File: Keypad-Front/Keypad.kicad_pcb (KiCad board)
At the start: 4 copper layers, 100.1 x 192.1 mm, 43 parts, among them J2 LED BOARD 1, J3 LED BOARD 2, J4 LED BOARD 3, J5 LED BOARD 4, J6 Conn_01x06, U1 DS3231MZ

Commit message: Back to a one-board design with rear-firing LEDs
Giving up on the UV LED idea for now.
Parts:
- removed J2: LED BOARD 1, Connector_PinHeader_2.54mm:PinHeader_2x02_P2.54mm_Vertical_SMD
- removed J3: LED BOARD 2, Connector_PinHeader_2.54mm:PinHeader_2x02_P2.54mm_Vertical_SMD
- removed J4: LED BOARD 3, Connector_PinHeader_2.54mm:PinHeader_2x02_P2.54mm_Vertical_SMD
- removed J5: LED BOARD 4, Connector_PinHeader_2.54mm:PinHeader_2x02_P2.54mm_Vertical_SMD
- removed R16: 4.7k, Resistor_SMD:R_0805_2012Metric_Pad1.20x1.40mm_HandSolder
- added BT1: Battery_Cell, Battery:BatteryHolder_MPD_BC2003_1x2032, B.Cu at (143.8, 194.3)
- added J1: RTC STEMMA QT, Transflective:JST-SH-4-VERT-SMD, B.Cu at (125.5, 204.3)
- added TP10: TestPoint, Keypad:Touch_Pad_D1.0mm, F.Cu at (81.5, 155.5)
- added TP11: TestPoint, Keypad:Touch_Pad_D1.0mm, F.Cu at (106.5, 155.5)
- added TP12: TestPoint, Keypad:Touch_Pad_D1.0mm, F.Cu at (131.5, 155.5)
- added TP14: Guard, Keypad:Touch_Pad_D1.0mm, B.Cu at (70.4, 76.2)
- added TP2: TestPoint, Keypad:Touch_Pad_D1.0mm, F.Cu at (106.5, 80.5)
- added TP3: TestPoint, Keypad:Touch_Pad_D1.0mm, F.Cu at (131.5, 80.5)
- added TP4: TestPoint, Keypad:Touch_Pad_D1.0mm, F.Cu at (81.5, 105.5)
- added TP5: TestPoint, Keypad:Touch_Pad_D1.0mm, F.Cu at (106.5, 105.5)
- added TP6: TestPoint, Keypad:Touch_Pad_D1.0mm, F.Cu at (131.5, 105.5)
- added TP7: TestPoint, Keypad:Touch_Pad_D1.0mm, F.Cu at (81.5, 130.5)
- added TP8: TestPoint, Keypad:Touch_Pad_D1.0mm, F.Cu at (106.5, 130.5)
- added TP9: TestPoint, Keypad:Touch_Pad_D1.0mm, F.Cu at (131.5, 130.5)
- added U3: CAP1214, Package_DFN_QFN:QFN-32-1EP_5x5mm_P0.5mm_EP3.3x3.3mm_ThermalVias, B.Cu at (108.5, 68.8)
- C1, C4, R13, R14, R17, R18, R19, U1: moved to B.Cu
- R1, R10, R11, R12, R2, R3, R4, R5, R6, R7, R8, R9: value 4.7k -> 100; moved to B.Cu
- R15: value 4.7k -> 0; moved to B.Cu
- TP1: value Guard -> TestPoint; footprint Capacitor_SMD:C_0805_2012Metric_Pad1.18x1.45mm_HandSolder -> Keypad:Touch_Pad_D1.0mm
- moved J6 288.7 mm to (20.2, 98.5)
- moved C2 274.9 mm to (33.5, 110.3)
- moved C3 274.9 mm to (33.5, 113.3)
- moved R17 264.4 mm to (38.8, 99.4), turned to 180 degrees
- moved R18 264.4 mm to (38.8, 102.3), turned to 180 degrees
- moved JP1 254.9 mm to (38.7, 107.6)
- moved R10 236.5 mm to (77.5, 162.1), turned to -90 degrees
- moved TP1 225.6 mm to (81.5, 80.5)
- moved R7 220.9 mm to (77.5, 137.1), turned to -90 degrees
- moved U1 219.9 mm to (125.7, 195.1), turned to -90 degrees
- moved R4 217.8 mm to (77.5, 112.1), turned to -90 degrees
- moved R1 215.9 mm to (77.5, 87.1), turned to -90 degrees
- moved R11 212.2 mm to (102.5, 162.1), turned to -90 degrees
- moved C1 210.8 mm to (130.8, 194.8), turned to -90 degrees
- moved R13 209.2 mm to (119.9, 194.8)
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- renumbered D3 to D1, D12 to D10, D10 to D12, D1 to D3, D6 to D4, D4 to D6, D9 to D7, D7 to D9
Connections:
- D1 pad 1: unconnected-(D1-K-Pad1) -> Net-(D1-K)
- D1 pad 2: unconnected-(D1-A-Pad2) -> /VLED
- D10 pad 1: unconnected-(D1-K-Pad1) -> Net-(D10-K)
- D10 pad 2: unconnected-(D1-A-Pad2) -> /VLED
- D11 pad 1: unconnected-(D1-K-Pad1) -> Net-(D11-K)
- D11 pad 2: unconnected-(D1-A-Pad2) -> /VLED
- D12 pad 1: unconnected-(D1-K-Pad1) -> Net-(D12-K)
- D12 pad 2: unconnected-(D1-A-Pad2) -> /VLED
- D2 pad 1: unconnected-(D1-K-Pad1) -> Net-(D2-K)
- D2 pad 2: unconnected-(D1-A-Pad2) -> /VLED
- D3 pad 1: unconnected-(D1-K-Pad1) -> Net-(D3-K)
- D3 pad 2: unconnected-(D1-A-Pad2) -> /VLED
- D4 pad 1: unconnected-(D1-K-Pad1) -> Net-(D4-K)
- D4 pad 2: unconnected-(D1-A-Pad2) -> /VLED
- D5 pad 1: unconnected-(D1-K-Pad1) -> Net-(D5-K)
- D5 pad 2: unconnected-(D1-A-Pad2) -> /VLED
- D6 pad 1: unconnected-(D1-K-Pad1) -> Net-(D6-K)
- D6 pad 2: unconnected-(D1-A-Pad2) -> /VLED
- D7 pad 1: unconnected-(D1-K-Pad1) -> Net-(D7-K)
- D7 pad 2: unconnected-(D1-A-Pad2) -> /VLED
- D8 pad 1: unconnected-(D1-K-Pad1) -> Net-(D8-K)
- D8 pad 2: unconnected-(D1-A-Pad2) -> /VLED
- D9 pad 1: unconnected-(D1-K-Pad1) -> Net-(D9-K)
- D9 pad 2: unconnected-(D1-A-Pad2) -> /VLED
- R1 pad 1: +5V -> /LED1
- R1 pad 2: /RTC_SDA -> Net-(D1-K)
- R10 pad 1: Net-(R10-Pad1) -> /LED10
- R10 pad 2: Net-(U3-CS8) -> Net-(D10-K)
- R11 pad 1: Net-(R11-Pad1) -> /LED11
- R11 pad 2: Net-(U3-CS9) -> Net-(D11-K)
- R12 pad 1: Net-(R12-Pad1) -> /LED12
- R12 pad 2: Net-(U3-CS10) -> Net-(D12-K)
- R13 pad 1: Net-(R13-Pad1) -> +5V
- R13 pad 2: Net-(U3-CS11) -> /RTC_SDA
- R14 pad 1: Net-(R14-Pad1) -> +5V
- R14 pad 2: Net-(U3-CS12) -> /RTC_SCL
- R15 pad 1: Net-(R15-Pad1) -> /LED12
- R15 pad 2: Net-(U3-CS13) -> /LED10
- R2 pad 1: +5V -> /LED2
- R2 pad 2: /RTC_SCL -> Net-(D2-K)
- R3 pad 1: Net-(R3-Pad1) -> /LED3
- R3 pad 2: Net-(U3-CS1) -> Net-(D3-K)
- R4 pad 1: Net-(R4-Pad1) -> /LED4
- R4 pad 2: Net-(U3-CS2) -> Net-(D4-K)
- R5 pad 1: Net-(R5-Pad1) -> /LED5
- R5 pad 2: Net-(U3-CS3) -> Net-(D5-K)
- R6 pad 1: Net-(R6-Pad1) -> /LED6
- R6 pad 2: Net-(U3-CS4) -> Net-(D6-K)
- R7 pad 1: Net-(R7-Pad1) -> /LED7
- R7 pad 2: Net-(U3-CS5) -> Net-(D7-K)
- R8 pad 1: Net-(R8-Pad1) -> /LED8
- R8 pad 2: Net-(U3-CS6) -> Net-(D8-K)
- R9 pad 1: Net-(R9-Pad1) -> /LED9
- R9 pad 2: Net-(U3-CS7) -> Net-(D9-K)
- TP1 pad 1: Net-(R3-Pad1) -> /TOUCH_1
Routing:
- net /VLED: track 0.00 -> 970.5 mm, vias 0 -> 12
- net /TOUCH_GUARD: track 0.00 -> 290.4 mm, vias 0 -> 5
- net /LED12: track 0.00 -> 225.1 mm, vias 0 -> 2
- net /TOUCH_10: track 0.00 -> 203.5 mm, vias 0 -> 3
- net /LED9: track 0.00 -> 196.4 mm, vias 0 -> 2
- net /LED11: track 0.00 -> 196.1 mm, vias 0 -> 2
- net /LED6: track 0.00 -> 170.7 mm, vias 0 -> 2
- net /TOUCH_11: track 0.00 -> 169.9 mm, vias 0 -> 1
- net /LED8: track 0.00 -> 169.5 mm, vias 0 -> 2
- net /TOUCH_7: track 0.00 -> 165.5 mm, vias 0 -> 1
- net /TOUCH_12: track 0.00 -> 152.2 mm, vias 0 -> 3
- net /LED3: track 0.00 -> 146.7 mm, vias 0 -> 2
- net /LED5: track 0.00 -> 144.1 mm, vias 0 -> 2
- net /LED10: track 0.00 -> 143.6 mm, vias 0 -> 2
- net /TOUCH_8: track 0.00 -> 141.6 mm, vias 0 -> 1
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
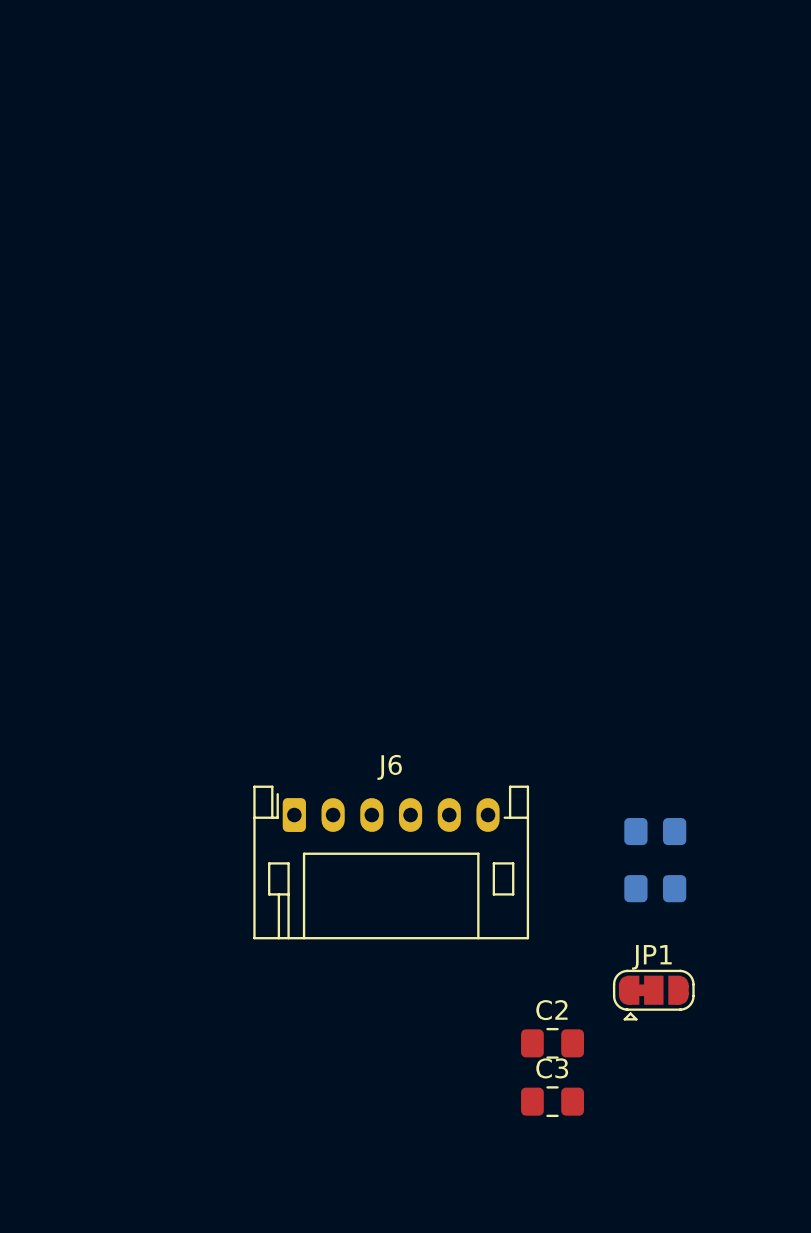
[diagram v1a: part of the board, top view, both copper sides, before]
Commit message: Steady work on Keypad PCB
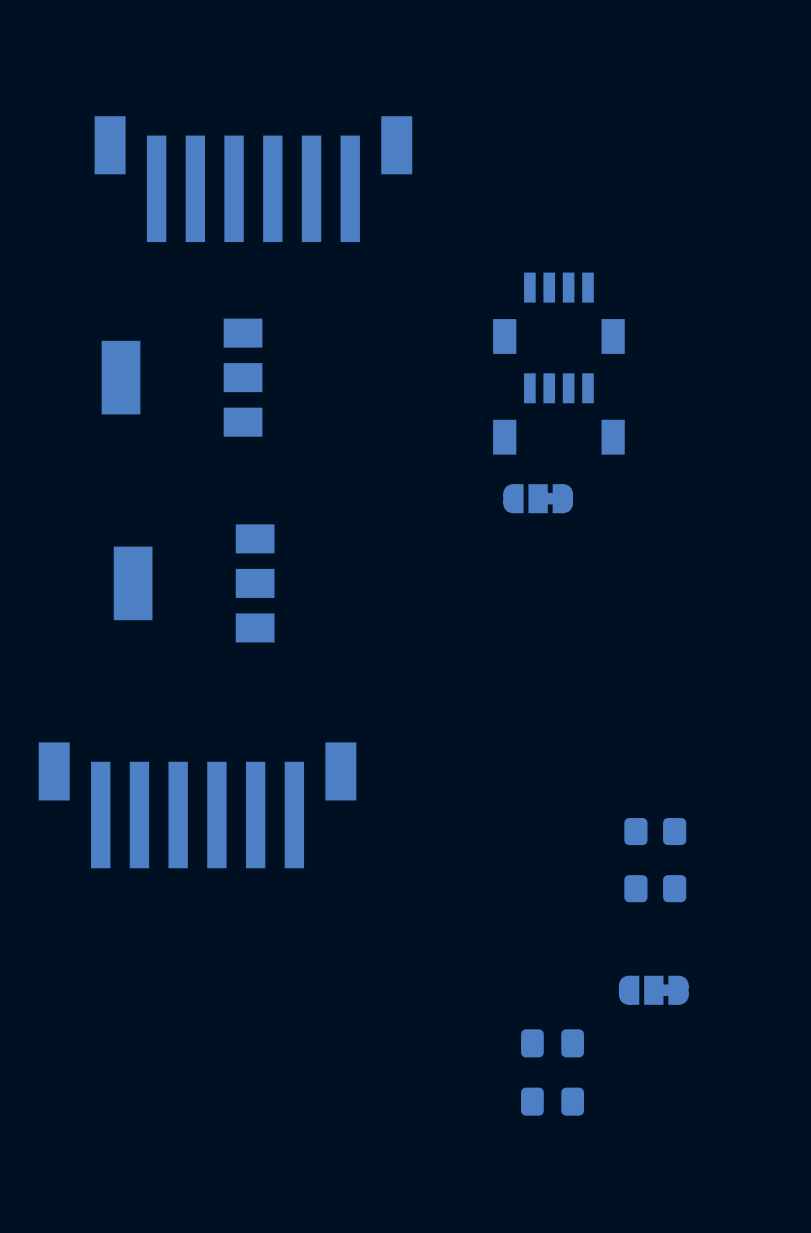
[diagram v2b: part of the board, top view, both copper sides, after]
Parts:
- added J10: EXP QWIIC, Transflective:JST-SH-4-VERT-SMD, B.Cu at (33.8, 71.3)
- added J11: TOUCH QWIIC, Transflective:JST-SH-4-VERT-SMD, B.Cu at (33.8, 76.5)
- added J7: JST-PH 6, Keypad:JST-PH-6-SMD, B.Cu at (23.1, 66.2)
- added J8: Feedback, Package_TO_SOT_SMD:SOT-223-3_TabPin2, B.Cu at (14.4, 75.9)
- added JP2: PWR SEL, Jumper:SolderJumper-3_P1.3mm_Bridged12_RoundedPad1.0x1.5mm, B.Cu at (32.8, 82.2)
- added U2: LM1117-3.3, Package_TO_SOT_SMD:SOT-223-3_TabPin2, B.Cu at (15.0, 86.6)
- C2, C3, JP1: moved to B.Cu
- J6: value Conn_01x06 -> JST-PH 6; footprint Connector_JST:JST_PH_S6B-PH-K_1x06_P2.00mm_Horizontal -> Keypad:JST-PH-6-SMD; moved to B.Cu
- turned C2 to 180 degrees
- turned C3 to 180 degrees
- turned J6 to 180 degrees
- turned JP1 to 180 degrees
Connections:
- net /VLED renamed /LED_VIN

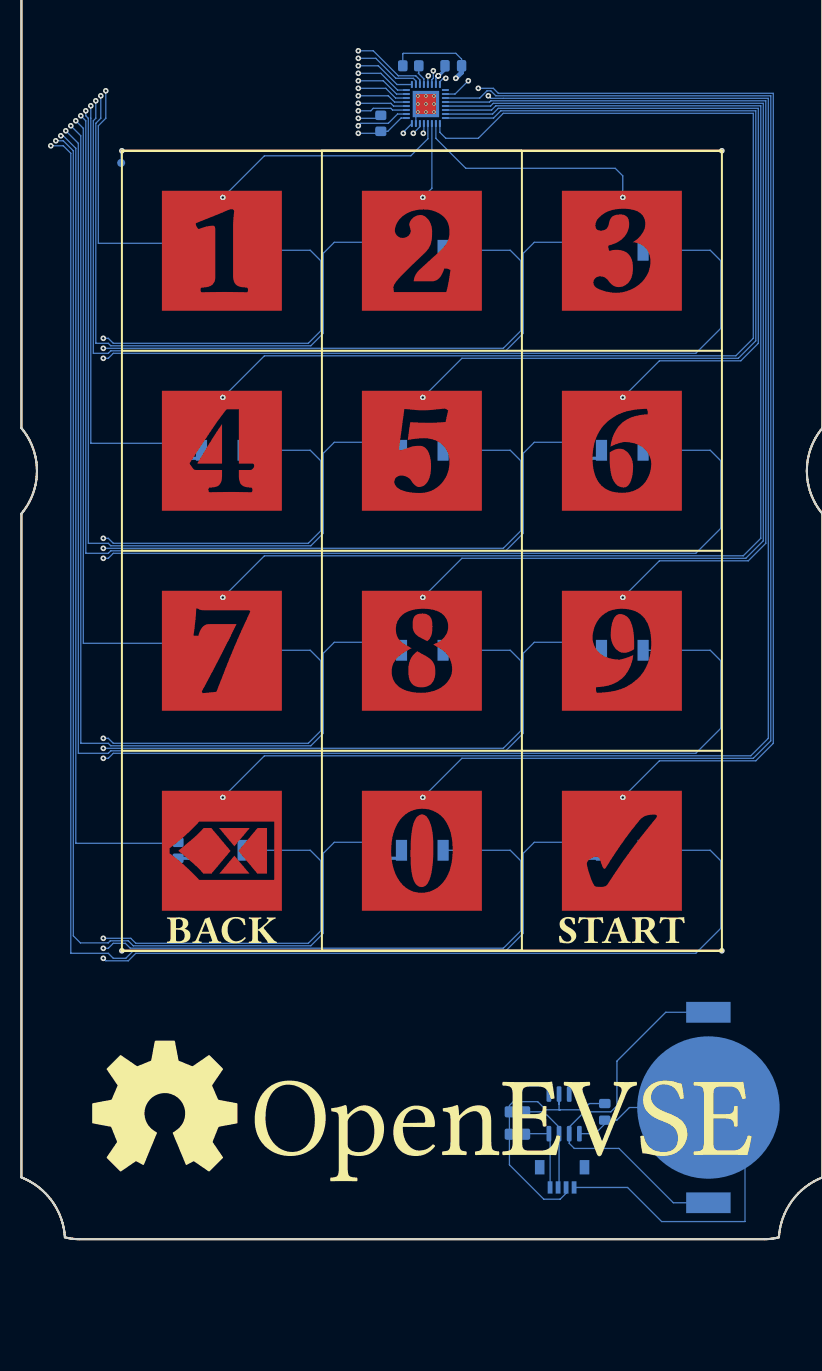
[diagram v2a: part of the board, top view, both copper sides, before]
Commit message: Attempt 2 at routing, cap sensor at bottom
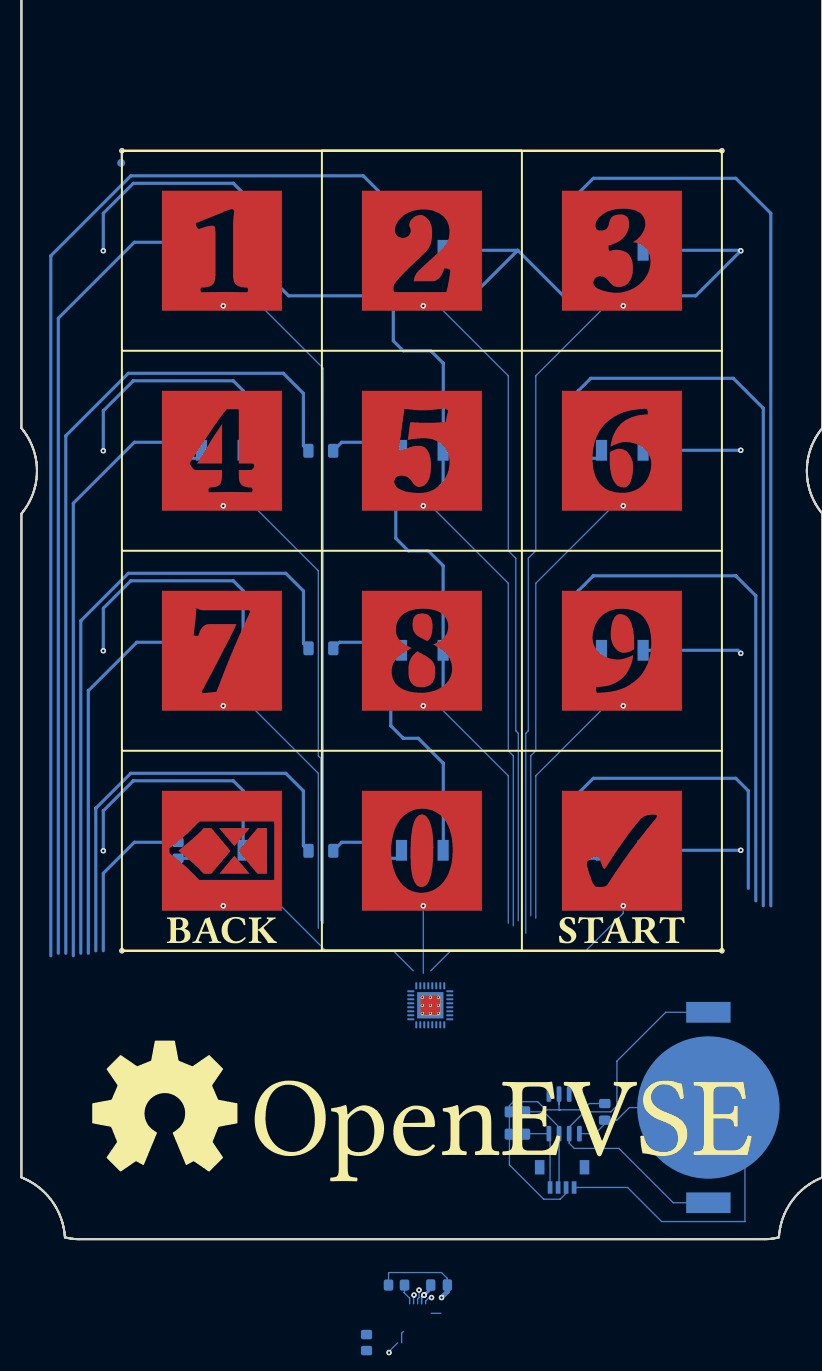
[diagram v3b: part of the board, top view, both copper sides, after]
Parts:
- added R16: 0, Resistor_SMD:R_1206_3216Metric_Pad1.30x1.75mm_HandSolder, B.Cu at (95.3, 112.2)
- added R20: 0, Resistor_SMD:R_1206_3216Metric_Pad1.30x1.75mm_HandSolder, B.Cu at (95.3, 136.9)
- added R21: 0, Resistor_SMD:R_1206_3216Metric_Pad1.30x1.75mm_HandSolder, B.Cu at (95.3, 162.2)
- moved C4 152.4 mm to (110.1, 216.5)
- moved R15 152.4 mm to (101.0, 223.7)
- moved R19 152.4 mm to (104.8, 216.5)
- moved U3 112.7 mm to (109.0, 181.5)
- moved TP1 13.5 mm to (81.6, 94.1)
- moved TP10 13.5 mm to (81.6, 169.1)
- moved TP11 13.5 mm to (106.6, 169.1)
- moved TP12 13.5 mm to (131.6, 169.1)
- moved TP2 13.5 mm to (106.6, 94.1)
- moved TP3 13.5 mm to (131.6, 94.1)
- moved TP4 13.5 mm to (81.6, 119.1)
- moved TP5 13.5 mm to (106.6, 119.1)
- moved TP6 13.5 mm to (131.6, 119.1)
- moved TP7 13.5 mm to (81.6, 144.1)
- moved TP8 13.5 mm to (106.6, 144.1)
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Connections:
- U3 pad 10: /LED11 -> Net-(U3-LED2)
- U3 pad 12: /LED8 -> Net-(U3-LED4)
- U3 pad 15: /LED5 -> Net-(U3-LED7)
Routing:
- net /LED_VIN: track 970.5 -> 507.3 mm, vias 12 -> 8
- net /LED11: track 196.1 -> 6.04 mm, vias 2 -> 0
- net /LED12: track 225.1 -> 41.0 mm, vias 2 -> 0
- net /TOUCH_10: track 203.5 -> 28.6 mm, vias 3 -> 1
- net /LED8: track 169.5 -> 5.91 mm, vias 2 -> 0
- net /TOUCH_11: track 169.9 -> 9.96 mm
- net /LED5: track 144.1 -> 6.05 mm, vias 2 -> 0
- net /TOUCH_7: track 165.5 -> 36.3 mm
- net /LED9: track 196.4 -> 68.6 mm, vias 2 -> 0
- net /LED10: track 143.6 -> 20.6 mm, vias 2 -> 0
- net /TOUCH_12: track 152.2 -> 29.5 mm, vias 3 -> 1
- net /TOUCH_8: track 141.6 -> 34.2 mm
- net Net-(U3-LED7): track 0.00 -> 106.1 mm
- net /TOUCH_9: track 117.6 -> 33.9 mm
- net /TOUCH_4: track 140.9 -> 60.6 mm
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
